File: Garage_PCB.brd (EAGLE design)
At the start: 35.6 x 44.4 mm, 19 parts, among them Q1 MOSFET-NCHANNELFQP30N06L

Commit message: Routed the traces
Routed all the traces for the board.  Ran a DRC and there were no
errors.
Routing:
- net LED2_O: track 0.00 -> 51.2 mm
- net LED_O: track 0.00 -> 38.8 mm
- net 24V: track 0.00 -> 14.3 mm
- net BTN_N: track 0.00 -> 13.0 mm
- net RNG_I: track 0.00 -> 10.3 mm
- net N$17: track 0.00 -> 9.65 mm
- net GND: track 0.00 -> 7.19 mm
- net N$15: track 0.00 -> 6.38 mm
- net RNG2_I: track 0.00 -> 6.35 mm
- net BTN_P: track 0.00 -> 5.45 mm
- net N$1: track 0.00 -> 4.97 mm
- net RD_SW_I: track 0.00 -> 4.49 mm
- net N$16: track 0.00 -> 3.98 mm

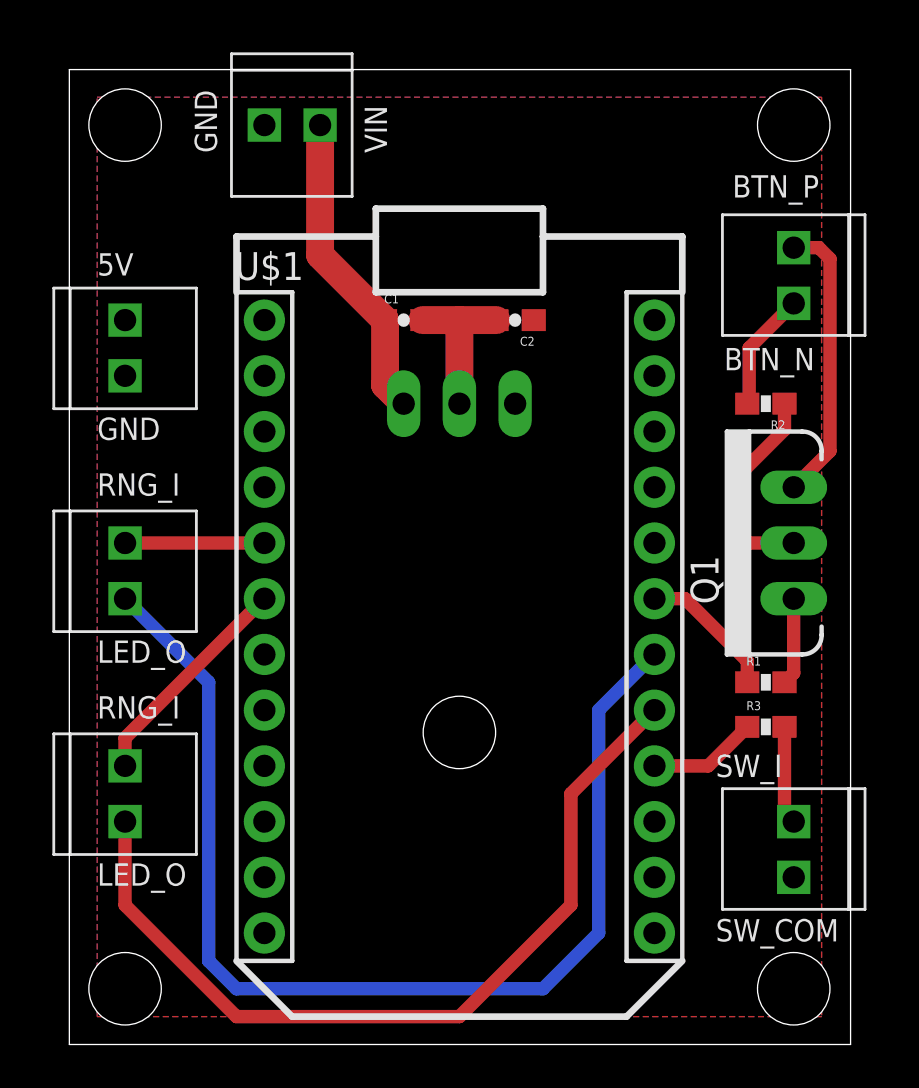
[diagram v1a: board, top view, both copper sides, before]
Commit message: Changed screw terminals to 3.5mm pitch instead of 2.54mm
These screw terminals are much less ugly but are a bit bigger.  They
still fit pretty well though.
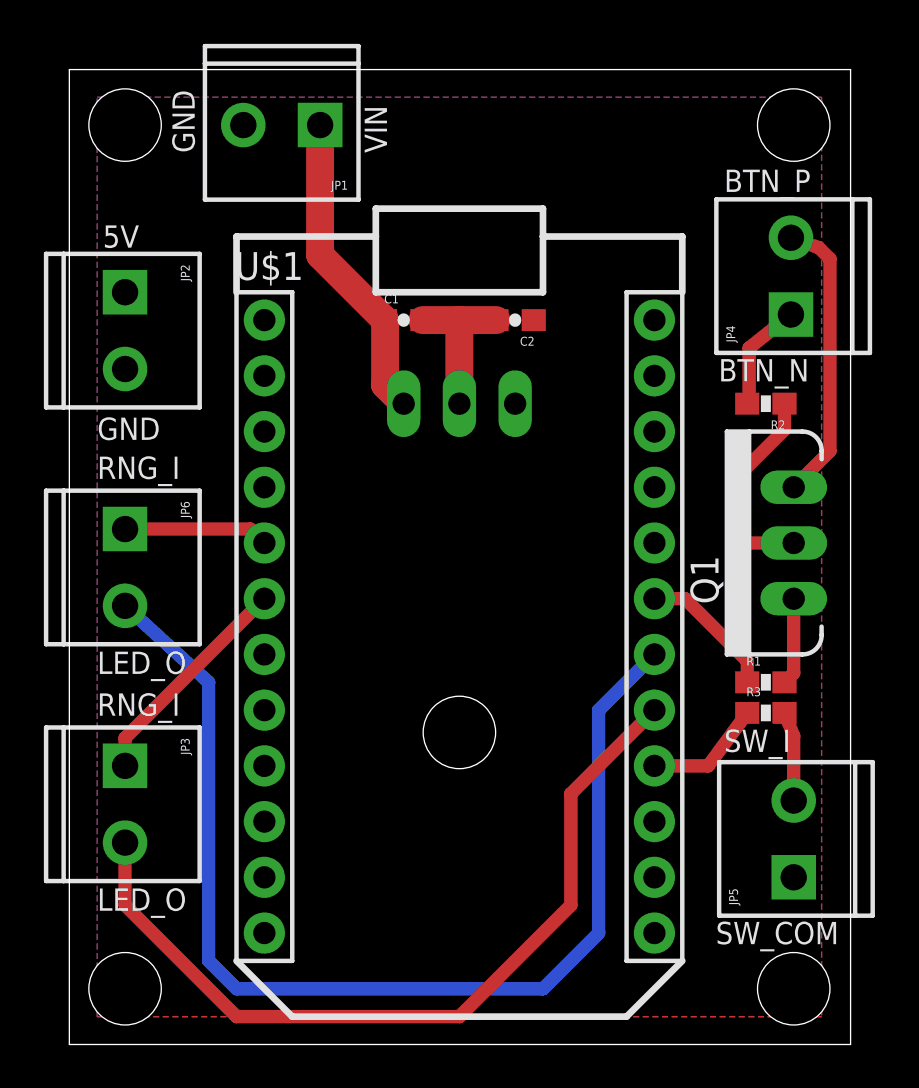
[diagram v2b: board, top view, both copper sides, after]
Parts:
- JP1, JP2, JP3, JP4, JP5, JP6: value M022.54MM_SCREWTERM -> M023.5MM; device Mikes-Stuff:1X02_2.54_SCREWTERM -> SparkFun-Connectors:SCREWTERMINAL-3.5MM-2
- moved JP2 3.81 mm to (2.54, 34.3), turned to 270 degrees
- moved JP6 3.18 mm to (2.54, 23.5), turned to 270 degrees
- moved JP4 3.05 mm to (32.9, 33.3), turned to 90 degrees
- moved JP5 2.54 mm to (33.0, 7.62), turned to 90 degrees
- moved JP1 2.54 mm to (11.4, 41.9), turned to 180 degrees
- moved JP3 2.54 mm to (2.54, 12.7), turned to 270 degrees
- moved R3 0.63 mm to (31.8, 15.1)
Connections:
- net 24V: now also JP1.1; no longer JP1.P1
- net 5V: now also JP2.1, JP5.1; no longer JP2.P1, JP5.P1
- net BTN_N: now also JP4.2; no longer JP4.P2
- net BTN_P: now also JP4.1; no longer JP4.P1
- net GND: now also JP1.2, JP2.2; no longer JP1.P2, JP2.P2
- net LED2_O: now also JP6.2; no longer JP6.P2
- net LED_O: now also JP3.2; no longer JP3.P2
- net RD_SW_I: now also JP5.2; no longer JP5.P2
- net RNG2_I: now also JP6.1; no longer JP6.P1
- net RNG_I: now also JP3.1; no longer JP3.P1
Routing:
- net LED_O: track 38.8 -> 37.8 mm
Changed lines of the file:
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@@
 <wire x1="35.611" y1="44.44" x2="0" y2="44.44" width="0" layer="20"/>
 <wire x1="0" y1="44.44" x2="0" y2="0" width="0" layer="20"/>
-<text x="1.27" y="35.052" size="1.016" layer="21" font="vector" ratio="15">5V</text>
+<text x="1.524" y="36.322" size="1.016" layer="21" font="vector" ratio="15">5V</text>
 <text x="1.27" y="27.559" size="1.016" layer="21" font="vector" ratio="15">GND</text>
-<text x="6.731" y="40.64" size="1.016" layer="21" font="vector" ratio="15" rot="R90">GND</text>
+<text x="5.715" y="40.64" size="1.016" layer="21" font="vector" ratio="15" rot="R90">GND</text>
 <text x="14.478" y="40.64" size="1.016" layer="21" font="vector" ratio="15" rot="R90">VIN</text>
-<text x="30.226" y="38.608" size="1.016" layer="21" font="vector" ratio="15">BTN_P</text>
-<text x="29.845" y="30.734" size="1.016" layer="21" font="vector" ratio="15">BTN_N</text>
-<text x="1.27" y="7.239" size="1.016" layer="21" font="vector" ratio="15">LED_O</text>
-<text x="1.27" y="14.859" size="1.016" layer="21" font="vector" ratio="15">RNG_I</text>
-<text x="29.464" y="4.699" size="1.016" layer="21" font="vector" ratio="15">SW_COM</text>
-<text x="29.464" y="12.192" size="1.016" layer="21" font="vector" ratio="15">SW_I</text>
-<text x="1.27" y="25.019" size="1.016" layer="21" font="vector" ratio="15">RNG_I</text>
-<text x="1.27" y="17.399" size="1.016" layer="21" font="vector" ratio="15">LED_O</text>
+<text x="29.845" y="38.862" size="1.016" layer="21" font="vector" ratio="15">BTN_P</text>
+<text x="29.591" y="30.226" size="1.016" layer="21" font="vector" ratio="15">BTN_N</text>
+<text x="1.27" y="6.096" size="1.016" layer="21" font="vector" ratio="15">LED_O</text>
+<text x="1.27" y="14.986" size="1.016" layer="21" font="vector" ratio="15">RNG_I</text>
+<text x="29.464" y="4.572" size="1.016" layer="21" font="vector" ratio="15">SW_COM</text>
+<text x="29.845" y="13.335" size="1.016" layer="21" font="vector" ratio="15">SW_I</text>
+<text x="1.27" y="25.781" size="1.016" layer="21" font="vector" ratio="15">RNG_I</text>
+<text x="1.27" y="16.891" size="1.016" layer="21" font="vector" ratio="15">LED_O</text>
 </plain>
 <attributes>
@@
 <element name="FRAME1" library="SparkFun-Aesthetics" package="CREATIVE_COMMONS" value="FRAME-LETTER" x="-77.47" y="49.53"/>
 <element name="U$1" library="Spark" package="SPARK_CORE" value="SPARK_CORECORE" x="17.78" y="19.05"/>
-<element name="JP1" library="Mikes-Stuff" package="1X02_2.54_SCREWTERM" value="M022.54MM_SCREWTERM" x="8.89" y="41.91"/>
-<element name="JP2" library="Mikes-Stuff" package="1X02_2.54_SCREWTERM" value="M022.54MM_SCREWTERM" x="2.54" y="30.48" rot="R90"/>
-<element name="JP3" library="Mikes-Stuff" package="1X02_2.54_SCREWTERM" value="M022.54MM_SCREWTERM" x="2.54" y="10.16" rot="R90"/>
-<element name="JP4" library="Mikes-Stuff" package="1X02_2.54_SCREWTERM" value="M022.54MM_SCREWTERM" x="33.02" y="36.322" rot="R270"/>
+<element name="JP1" library="SparkFun-Connectors" package="SCREWTERMINAL-3.5MM-2" value="M023.5MM" x="11.43" y="41.91" rot="R180"/>
+<element name="JP2" library="SparkFun-Connectors" package="SCREWTERMINAL-3.5MM-2" value="M023.5MM" x="2.54" y="34.29" rot="R270"/>
+<element name="JP3" library="SparkFun-Connectors" package="SCREWTERMINAL-3.5MM-2" value="M023.5MM" x="2.54" y="12.7" rot="R270"/>
+<element name="JP4" library="SparkFun-Connectors" package="SCREWTERMINAL-3.5MM-2" value="M023.5MM" x="32.893" y="33.274" rot="R90"/>
 <element name="Q1" library="SparkFun-DiscreteSemi" package="TO220V" value="MOSFET-NCHANNELFQP30N06L" x="33.02" y="22.86" rot="R90">
 <attribute name="PROD_ID" value="TRANS-10060" x="76.2" y="60.96" size="1.778" layer="27" rot="R90" display="off"/>
@@
 <element name="C2" library="SparkFun-Capacitors" package="0603-CAP" value="" x="20.32" y="33.02" rot="R180"/>
 <element name="R2" library="SparkFun-Resistors" package="0603-RES" value="1K" x="31.75" y="29.21" rot="R180"/>
-<element name="JP5" library="Mikes-Stuff" package="1X02_2.54_SCREWTERM" value="M022.54MM_SCREWTERM" x="33.02" y="10.16" rot="R270"/>
-<element name="R3" library="SparkFun-Resistors" package="0603-RES" value="" x="31.75" y="14.478"/>
+<element name="JP5" library="SparkFun-Connectors" package="SCREWTERMINAL-3.5MM-2" value="M023.5MM" x="33.02" y="7.62" rot="R90"/>
+<element name="R3" library="SparkFun-Resistors" package="0603-RES" value="" x="31.75" y="15.113"/>
 <element name="STANDOFF1" library="SparkFun-Electromechanical" package="STAND-OFF" value="STAND-OFF" x="2.54" y="2.54"/>
 <element name="STANDOFF2" library="SparkFun-Electromechanical" package="STAND-OFF" value="STAND-OFF" x="33.02" y="2.54"/>
 <element name="STANDOFF3" library="SparkFun-Electromechanical" package="STAND-OFF" value="STAND-OFF" x="2.54" y="41.91"/>
 <element name="STANDOFF4" library="SparkFun-Electromechanical" package="STAND-OFF" value="STAND-OFF" x="33.02" y="41.91"/>
-<element name="JP6" library="Mikes-Stuff" package="1X02_2.54_SCREWTERM" value="M022.54MM_SCREWTERM" x="2.54" y="20.32" rot="R90"/>
+<element name="JP6" library="SparkFun-Connectors" package="SCREWTERMINAL-3.5MM-2" value="M023.5MM" x="2.54" y="23.495" rot="R270"/>
 </elements>
 <signals>
@@
 </signal>
 <signal name="BTN_P">
-<contactref element="JP4" pad="P1"/>
+<contactref element="JP4" pad="1"/>
 <contactref element="R2" pad="2"/>
-<wire x1="33.02" y1="33.782" x2="30.988" y2="31.75" width="0.6096" layer="1"/>
+<wire x1="32.893" y1="33.274" x2="30.988" y2="31.75" width="0.6096" layer="1"/>
 <wire x1="30.988" y1="31.75" x2="30.988" y2="29.298" width="0.6096" layer="1"/>
 <wire x1="30.988" y1="29.298" x2="30.9" y2="29.21" width="0.254" layer="1"/>
 </signal>
 <signal name="BTN_N">
-<contactref element="JP4" pad="P2"/>
+<contactref element="JP4" pad="2"/>
 <contactref element="Q1" pad="3"/>
-<wire x1="33.02" y1="36.322" x2="34.163" y2="36.322" width="0.6096" layer="1"/>
+<wire x1="32.893" y1="36.774" x2="34.163" y2="36.322" width="0.6096" layer="1"/>
 <wire x1="34.163" y1="36.322" x2="34.671" y2="35.814" width="0.6096" layer="1"/>
 <wire x1="34.671" y1="35.814" x2="34.671" y2="27.051" width="0.6096" layer="1"/>
@@
 </signal>
 <signal name="LED_O">
-<contactref element="JP3" pad="P2"/>
+<contactref element="JP3" pad="2"/>
 <contactref element="U$1" pad="17"/>
-<wire x1="2.54" y1="10.16" x2="2.54" y2="6.35" width="0.6096" layer="1"/>
+<wire x1="2.54" y1="9.2" x2="2.54" y2="6.35" width="0.6096" layer="1"/>
 <wire x1="2.54" y1="6.35" x2="7.62" y2="1.27" width="0.6096" layer="1"/>
 <wire x1="7.62" y1="1.27" x2="17.78" y2="1.27" width="0.6096" layer="1"/>
@@
 <signal name="RNG_I">
 <contactref element="U$1" pad="6"/>
-<contactref element="JP3" pad="P1"/>
+<contactref element="JP3" pad="1"/>
 <wire x1="2.54" y1="12.7" x2="2.54" y2="13.97" width="0.6096" layer="1"/>
 <wire x1="2.54" y1="13.97" x2="8.89" y2="20.32" width="0.6096" layer="1"/>
@@
 <contactref element="IC1" pad="IN"/>
 <contactref element="C1" pad="1"/>
-<contactref element="JP1" pad="P1"/>
+<contactref element="JP1" pad="1"/>
 <wire x1="11.43" y1="41.91" x2="11.43" y2="35.98" width="1.27" layer="1"/>
 <wire x1="11.43" y1="35.98" x2="14.39" y2="33.02" width="1.27" layer="1"/>
@@
 <contactref element="C2" pad="2"/>
 <contactref element="IC1" pad="GND"/>
-<contactref element="JP1" pad="P2"/>
-<contactref element="JP2" pad="P2"/>
+<contactref element="JP1" pad="2"/>
+<contactref element="JP2" pad="2"/>
 <contactref element="U$1" pad="2"/>
 <contactref element="U$1" pad="21"/>
@@
 <contactref element="IC1" pad="OUT"/>
 <contactref element="C2" pad="1"/>
-<contactref element="JP2" pad="P1"/>
+<contactref element="JP2" pad="1"/>
 <contactref element="U$1" pad="1"/>
-<contactref element="JP5" pad="P1"/>
+<contactref element="JP5" pad="1"/>
 <polygon width="0.254" layer="1">
 <vertex x="1.27" y="43.18"/>
@@
 </signal>
 <signal name="RD_SW_I">
-<contactref element="JP5" pad="P2"/>
+<contactref element="JP5" pad="2"/>
 <contactref element="R3" pad="2"/>
-<wire x1="32.6" y1="14.478" x2="32.6" y2="10.58" width="0.6096" layer="1"/>
-<wire x1="32.6" y1="10.58" x2="33.02" y2="10.16" width="0.6096" layer="1"/>
+<wire x1="32.6" y1="15.113" x2="33.02" y2="14.058" width="0.6096" layer="1"/>
+<wire x1="33.02" y1="14.058" x2="33.02" y2="11.12" width="0.6096" layer="1"/>
 </signal>
 <signal name="N$1">
@@
 <contactref element="R3" pad="1"/>
 <wire x1="26.67" y1="12.7" x2="29.122" y2="12.7" width="0.6096" layer="1"/>
-<wire x1="29.122" y1="12.7" x2="30.9" y2="14.478" width="0.6096" layer="1"/>
+<wire x1="29.122" y1="12.7" x2="30.9" y2="15.113" width="0.6096" layer="1"/>
 </signal>
 <signal name="RNG2_I">
-<contactref element="JP6" pad="P1"/>
+<contactref element="JP6" pad="1"/>
 <contactref element="U$1" pad="5"/>
-<wire x1="2.54" y1="22.86" x2="8.89" y2="22.86" width="0.6096" layer="1"/>
+<wire x1="8.89" y1="22.86" x2="8.255" y2="23.495" width="0.6096" layer="1"/>
+<wire x1="8.255" y1="23.495" x2="2.54" y2="23.495" width="0.6096" layer="1"/>
 </signal>
 <signal name="LED2_O">
 <contactref element="U$1" pad="18"/>
-<contactref element="JP6" pad="P2"/>
-<wire x1="2.54" y1="20.32" x2="6.35" y2="16.51" width="0.6096" layer="16"/>
+<contactref element="JP6" pad="2"/>
+<wire x1="2.54" y1="19.995" x2="6.35" y2="16.51" width="0.6096" layer="16"/>
 <wire x1="6.35" y1="16.51" x2="6.35" y2="3.81" width="0.6096" layer="16"/>
 <wire x1="6.35" y1="3.81" x2="7.62" y2="2.54" width="0.6096" layer="16"/>

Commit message: Put 5V regulator on top layer
Moved the regulator from the bottom layer to the top layer.  It is still
underneath the Spark but there should be plenty of room for it.
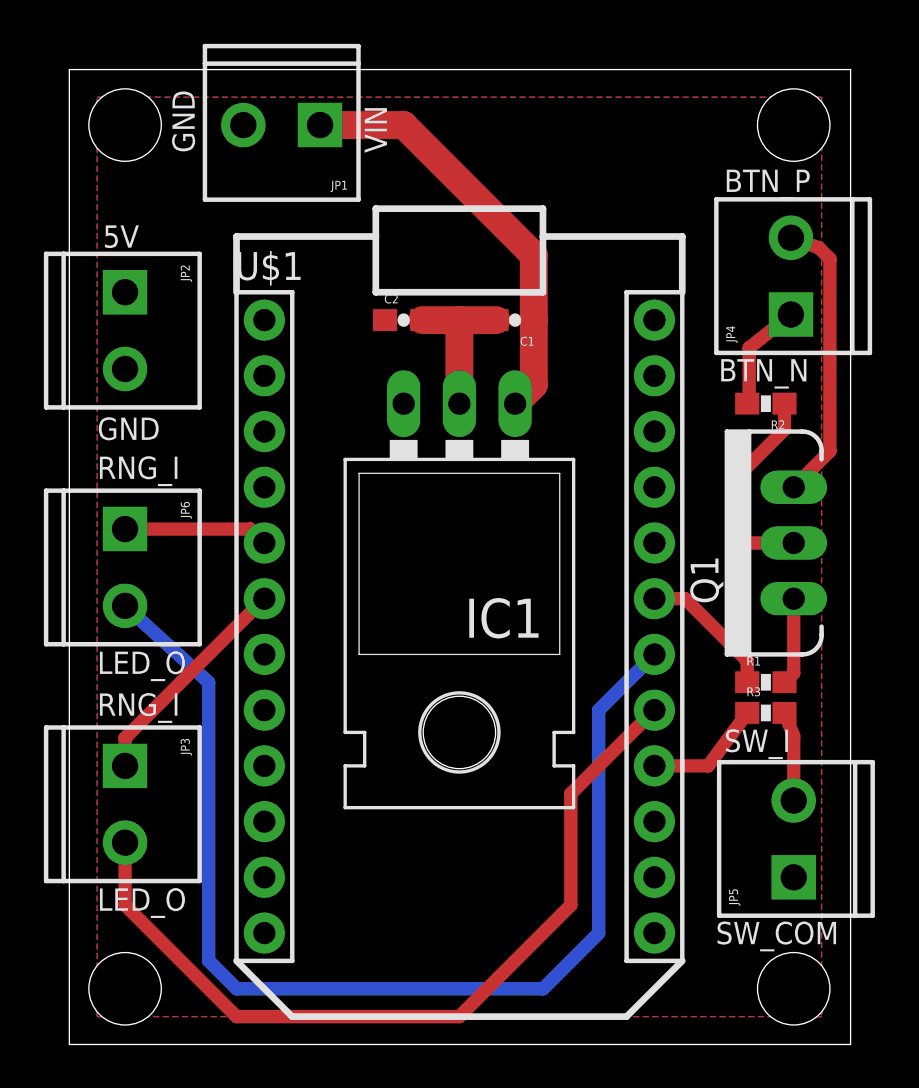
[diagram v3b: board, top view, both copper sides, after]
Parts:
- moved C1 5.08 mm to (20.3, 33.0), turned to 180 degrees
- moved C2 5.08 mm to (15.2, 33.0), turned to 0 degrees
- flipped IC1 to the top
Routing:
- net 24V: track 14.3 -> 19.3 mm
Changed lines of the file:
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@@
 </element>
 <element name="R1" library="SparkFun-Resistors" package="0603-RES" value="10K" x="31.75" y="16.51"/>
-<element name="IC1" library="SparkFun-PowerIC" package="TO-220-ALT" value="" x="17.78" y="25.4" rot="MR180"/>
-<element name="C1" library="SparkFun-Capacitors" package="0603-CAP" value="" x="15.24" y="33.02"/>
-<element name="C2" library="SparkFun-Capacitors" package="0603-CAP" value="" x="20.32" y="33.02" rot="R180"/>
+<element name="IC1" library="SparkFun-PowerIC" package="TO-220-ALT" value="" x="17.78" y="25.4" rot="R180"/>
+<element name="C1" library="SparkFun-Capacitors" package="0603-CAP" value="" x="20.32" y="33.02" rot="R180"/>
+<element name="C2" library="SparkFun-Capacitors" package="0603-CAP" value="" x="15.24" y="33.02"/>
 <element name="R2" library="SparkFun-Resistors" package="0603-RES" value="1K" x="31.75" y="29.21" rot="R180"/>
 <element name="JP5" library="SparkFun-Connectors" package="SCREWTERMINAL-3.5MM-2" value="M023.5MM" x="33.02" y="7.62" rot="R90"/>
@@
 <contactref element="C1" pad="1"/>
 <contactref element="JP1" pad="1"/>
-<wire x1="11.43" y1="41.91" x2="11.43" y2="35.98" width="1.27" layer="1"/>
-<wire x1="11.43" y1="35.98" x2="14.39" y2="33.02" width="1.27" layer="1"/>
-<wire x1="15.24" y1="29.21" x2="14.39" y2="30.06" width="1.27" layer="1"/>
-<wire x1="14.39" y1="30.06" x2="14.39" y2="33.02" width="1.27" layer="1"/>
+<wire x1="21.17" y1="33.02" x2="21.17" y2="30.06" width="1.27" layer="1"/>
+<wire x1="21.17" y1="30.06" x2="20.32" y2="29.21" width="1.27" layer="1"/>
+<wire x1="21.17" y1="33.02" x2="21.17" y2="35.98" width="1.27" layer="1"/>
+<wire x1="21.17" y1="35.98" x2="15.24" y2="41.91" width="1.27" layer="1"/>
+<wire x1="15.24" y1="41.91" x2="11.43" y2="41.91" width="1.27" layer="1"/>
 </signal>
 <signal name="GND">
@@
 <contactref element="U$1" pad="1"/>
 <contactref element="JP5" pad="1"/>
-<polygon width="0.254" layer="1">
+<polygon width="0.254" layer="1" thermals="no">
 <vertex x="1.27" y="43.18"/>
 <vertex x="34.29" y="43.18"/>
